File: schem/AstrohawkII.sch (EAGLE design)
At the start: 4 parts, among them J1 RASPBERRYPI-40-PIN-GPIO_PTH_N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

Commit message: updates eagle schematic and board
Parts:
- removed J3: (no value), SparkFun-Connectors:CONN_04PTH
- removed J4: (no value), SparkFun-Connectors:CONN_06SILK_FEMALE_PTH
- added U$1: BNO055, rocketry:BNO055
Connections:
- removed net 3VO: J2.3, J4.2
- removed net ADR: J3.4
- removed net PS0: J3.1
- removed net PS1: J3.2
- net GND: no longer J4.3
- net INT: now also J1.GP5; no longer J3.3
- net INT1: now also J1.GP12
- net INT2: now also J1.GP13
- net RST: now also J1.GP6; no longer J4.6
- net SCL: no longer J4.5
- net SDA: no longer J4.4
- net VIN: no longer J4.1
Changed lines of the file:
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@@
 <attribute name="MPL3115A2" value=""/>
 </part>
-<part name="J3" library="SparkFun-Connectors" deviceset="CONN_04" device="PTH">
-<attribute name="BNO055X04" value=""/>
-</part>
-<part name="J4" library="SparkFun-Connectors" deviceset="CONN_06" device="SILK_FEMALE_PTH">
-<attribute name="BNO055X06" value=""/>
-</part>
+<part name="U$1" library="rocketry" deviceset="BNO055" device=""/>
 </parts>
 <sheets>
@@
 <attribute name="MPL3115A2" x="73.66" y="78.74" size="1.778" layer="96" display="name"/>
 </instance>
-<instance part="J3" gate="J1" x="78.74" y="66.04" smashed="yes">
-<attribute name="VALUE" x="73.66" y="58.674" size="1.778" layer="96" font="vector"/>
-<attribute name="NAME" x="73.66" y="74.168" size="1.778" layer="95" font="vector"/>
-<attribute name="BNO055X04" x="73.66" y="58.42" size="1.778" layer="96" display="name"/>
-</instance>
-<instance part="J4" gate="G$1" x="78.74" y="43.18" smashed="yes">
-<attribute name="VALUE" x="73.66" y="33.274" size="1.778" layer="96" font="vector"/>
-<attribute name="NAME" x="73.66" y="53.848" size="1.778" layer="95" font="vector"/>
-<attribute name="BNO055X06" x="73.66" y="33.02" size="1.778" layer="96" display="name"/>
+<instance part="U$1" gate="G$1" x="116.84" y="35.56" smashed="yes">
+<attribute name="NAME" x="114.3" y="58.42" size="1.778" layer="95"/>
+<attribute name="VALUE" x="114.3" y="17.78" size="1.778" layer="96"/>
 </instance>
 </instances>
@@
 <net name="PS0" class="0">
 <segment>
-<pinref part="J3" gate="J1" pin="1"/>
-<wire x1="83.82" y1="63.5" x2="91.44" y2="63.5" width="0.1524" layer="91"/>
-<label x="88.9" y="63.5" size="1.778" layer="95" align="bottom-right"/>
+<wire x1="137.16" y1="48.26" x2="144.78" y2="48.26" width="0.1524" layer="91"/>
+<label x="149.86" y="48.26" size="1.778" layer="95" align="bottom-right"/>
 </segment>
 </net>
 <net name="PS1" class="0">
 <segment>
-<pinref part="J3" gate="J1" pin="2"/>
-<wire x1="83.82" y1="66.04" x2="91.44" y2="66.04" width="0.1524" layer="91"/>
-<label x="88.9" y="66.04" size="1.778" layer="95" align="bottom-right"/>
+<wire x1="137.16" y1="43.18" x2="144.78" y2="43.18" width="0.1524" layer="91"/>
+<label x="149.86" y="43.18" size="1.778" layer="95" align="bottom-right"/>
 </segment>
 </net>
 <net name="INT" class="0">
 <segment>
-<pinref part="J3" gate="J1" pin="3"/>
-<wire x1="83.82" y1="68.58" x2="91.44" y2="68.58" width="0.1524" layer="91"/>
-<label x="88.9" y="68.58" size="1.778" layer="95" align="bottom-right"/>
+<wire x1="137.16" y1="38.1" x2="144.78" y2="38.1" width="0.1524" layer="91"/>
+<label x="149.86" y="38.1" size="1.778" layer="95" align="bottom-right"/>
+</segment>
+<segment>
+<pinref part="J1" gate="G$1" pin="GP5"/>
+<wire x1="10.16" y1="86.36" x2="2.54" y2="86.36" width="0.1524" layer="91"/>
+<label x="0" y="86.36" size="1.778" layer="95"/>
 </segment>
 </net>
 <net name="ADR" class="0">
 <segment>
-<pinref part="J3" gate="J1" pin="4"/>
-<wire x1="83.82" y1="71.12" x2="91.44" y2="71.12" width="0.1524" layer="91"/>
-<label x="88.9" y="71.12" size="1.778" layer="95" align="bottom-right"/>
+<wire x1="137.16" y1="33.02" x2="144.78" y2="33.02" width="0.1524" layer="91"/>
+<label x="144.78" y="33.02" size="1.778" layer="95" rot="MR0" align="bottom-right"/>
 </segment>
 </net>
@@
 </segment>
 <segment>
-<pinref part="J4" gate="G$1" pin="1"/>
-<wire x1="83.82" y1="38.1" x2="91.44" y2="38.1" width="0.1524" layer="91"/>
-<label x="88.9" y="38.1" size="1.778" layer="95" align="bottom-right"/>
+<wire x1="93.98" y1="50.8" x2="101.6" y2="50.8" width="0.1524" layer="91"/>
+<label x="93.98" y="50.8" size="1.778" layer="95" align="bottom-right"/>
 </segment>
 <segment>
@@
 </segment>
 <segment>
-<pinref part="J4" gate="G$1" pin="3"/>
-<wire x1="83.82" y1="43.18" x2="91.44" y2="43.18" width="0.1524" layer="91"/>
-<label x="88.9" y="43.18" size="1.778" layer="95" align="bottom-right"/>
+<wire x1="93.98" y1="40.64" x2="101.6" y2="40.64" width="0.1524" layer="91"/>
+<label x="93.98" y="40.64" size="1.778" layer="95" align="bottom-right"/>
 </segment>
 <segment>
@@
 <wire x1="10.16" y1="43.18" x2="-5.08" y2="43.18" width="0.1524" layer="91"/>
 <label x="-2.54" y="43.18" size="1.778" layer="95"/>
-</segment>
-</net>
-<net name="3VO" class="0">
-<segment>
-<pinref part="J2" gate="J1" pin="3"/>
-<wire x1="83.82" y1="88.9" x2="91.44" y2="88.9" width="0.1524" layer="91"/>
-<label x="88.9" y="88.9" size="1.778" layer="95" align="bottom-right"/>
-</segment>
-<segment>
-<pinref part="J4" gate="G$1" pin="2"/>
-<wire x1="83.82" y1="40.64" x2="91.44" y2="40.64" width="0.1524" layer="91"/>
-<label x="88.9" y="40.64" size="1.778" layer="95" align="bottom-right"/>
 </segment>
 </net>
@@
 <label x="88.9" y="91.44" size="1.778" layer="95" align="bottom-right"/>
 </segment>
+<segment>
+<pinref part="J1" gate="G$1" pin="GP13"/>
+<wire x1="10.16" y1="78.74" x2="2.54" y2="78.74" width="0.1524" layer="91"/>
+<label x="0" y="78.74" size="1.778" layer="95"/>
+</segment>
 </net>
 <net name="INT1" class="0">
@@
 <wire x1="83.82" y1="93.98" x2="91.44" y2="93.98" width="0.1524" layer="91"/>
 <label x="88.9" y="93.98" size="1.778" layer="95" align="bottom-right"/>
+</segment>
+<segment>
+<pinref part="J1" gate="G$1" pin="GP12"/>
+<wire x1="10.16" y1="81.28" x2="2.54" y2="81.28" width="0.1524" layer="91"/>
+<label x="0" y="81.28" size="1.778" layer="95"/>
 </segment>
 </net>
@@
 </segment>
 <segment>
-<pinref part="J4" gate="G$1" pin="5"/>
-<wire x1="83.82" y1="48.26" x2="91.44" y2="48.26" width="0.1524" layer="91"/>
-<label x="88.9" y="48.26" size="1.778" layer="95" align="bottom-right"/>
+<wire x1="93.98" y1="30.48" x2="101.6" y2="30.48" width="0.1524" layer="91"/>
+<label x="93.98" y="30.48" size="1.778" layer="95" align="bottom-right"/>
 </segment>
 <segment>
@@
 </segment>
 <segment>
-<pinref part="J4" gate="G$1" pin="4"/>
-<wire x1="83.82" y1="45.72" x2="91.44" y2="45.72" width="0.1524" layer="91"/>
-<label x="88.9" y="45.72" size="1.778" layer="95" align="bottom-right"/>
+<wire x1="93.98" y1="35.56" x2="101.6" y2="35.56" width="0.1524" layer="91"/>
+<label x="93.98" y="35.56" size="1.778" layer="95" align="bottom-right"/>
 </segment>
 <segment>
@@
 <net name="RST" class="0">
 <segment>
-<pinref part="J4" gate="G$1" pin="6"/>
-<wire x1="83.82" y1="50.8" x2="91.44" y2="50.8" width="0.1524" layer="91"/>
-<label x="88.9" y="50.8" size="1.778" layer="95" align="bottom-right"/>
+<wire x1="93.98" y1="25.4" x2="101.6" y2="25.4" width="0.1524" layer="91"/>
+<label x="93.98" y="25.4" size="1.778" layer="95" align="bottom-right"/>
+</segment>
+<segment>
+<pinref part="J1" gate="G$1" pin="GP6"/>
+<wire x1="10.16" y1="83.82" x2="2.54" y2="83.82" width="0.1524" layer="91"/>
+<label x="0" y="83.82" size="1.778" layer="95"/>
 </segment>
 </net>

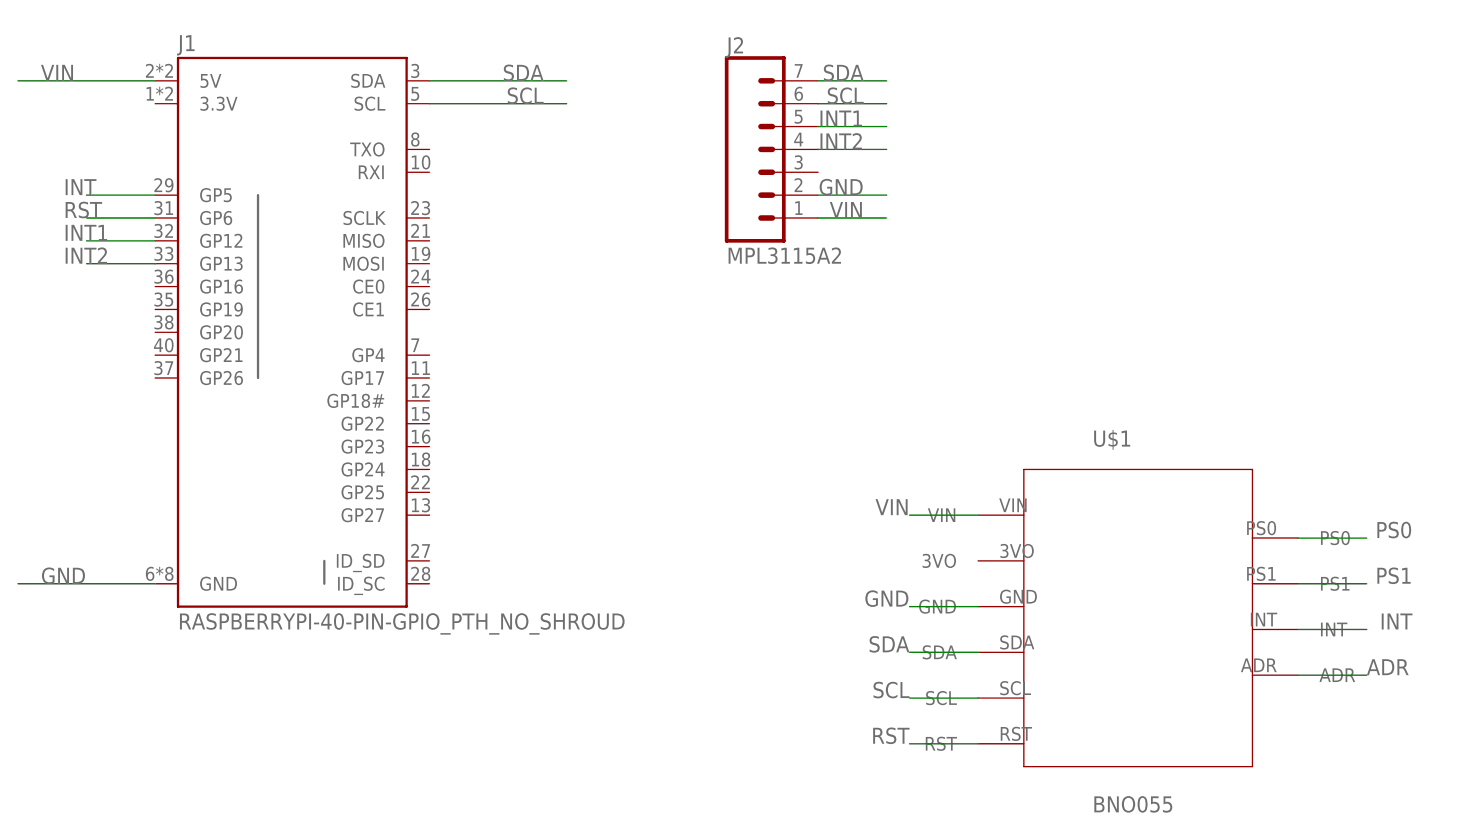
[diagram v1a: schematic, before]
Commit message: fixes holes for raspberry pi
This change fixes the holes for the raspberry pi, adds
measurement lines showing the correct dimensions, and
updates the IMU part because the pins were backwards on
the symbol.
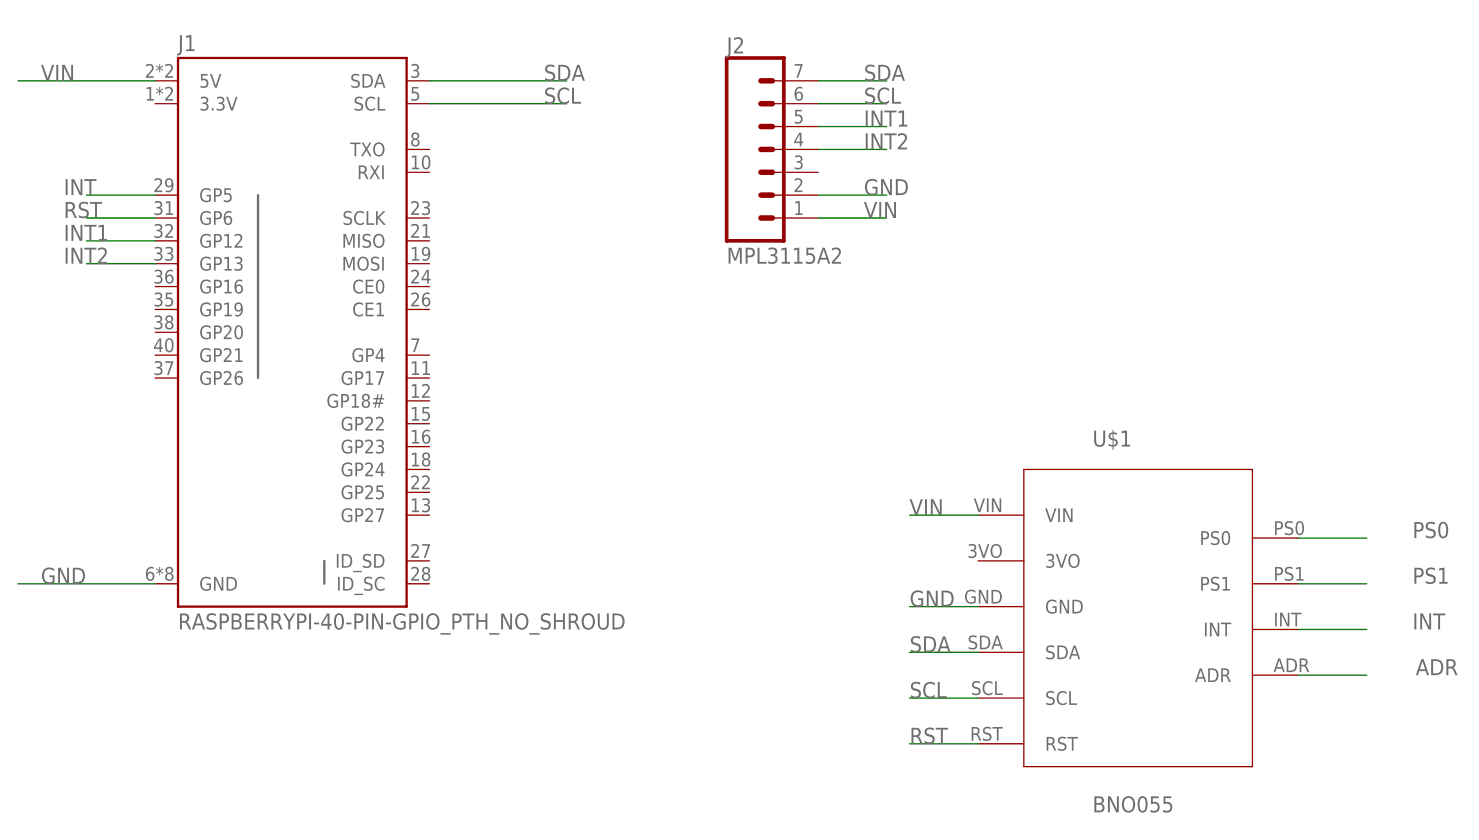
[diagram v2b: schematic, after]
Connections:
- new net ADR: U$1.ADR
- new net PS0: U$1.PS0
- new net PS1: U$1.PS1
- net GND: now also U$1.GND
- net INT: now also U$1.INT
- net RST: now also U$1.RST
- net SCL: now also U$1.SCL
- net SDA: now also U$1.SDA
- net VIN: now also U$1.VIN
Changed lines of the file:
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@@
 <?xml version="1.0" encoding="utf-8"?>
 <!DOCTYPE eagle SYSTEM "eagle.dtd">
-<eagle version="9.5.2">
+<eagle version="8.2.2">
 <drawing>
 <settings>
@@
 <attribute name="MPL3115A2" x="73.66" y="78.74" size="1.778" layer="96" display="name"/>
 </instance>
-<instance part="U$1" gate="G$1" x="116.84" y="35.56" smashed="yes">
-<attribute name="NAME" x="114.3" y="58.42" size="1.778" layer="95"/>
-<attribute name="VALUE" x="114.3" y="17.78" size="1.778" layer="96"/>
-</instance>
+<instance part="U$1" gate="G$1" x="116.84" y="35.56"/>
 </instances>
 <busses>
@@
 <segment>
 <wire x1="137.16" y1="48.26" x2="144.78" y2="48.26" width="0.1524" layer="91"/>
-<label x="149.86" y="48.26" size="1.778" layer="95" align="bottom-right"/>
+<label x="149.86" y="48.26" size="1.778" layer="95"/>
+<pinref part="U$1" gate="G$1" pin="PS0"/>
 </segment>
 </net>
@@
 <segment>
 <wire x1="137.16" y1="43.18" x2="144.78" y2="43.18" width="0.1524" layer="91"/>
-<label x="149.86" y="43.18" size="1.778" layer="95" align="bottom-right"/>
+<label x="149.86" y="43.18" size="1.778" layer="95"/>
+<pinref part="U$1" gate="G$1" pin="PS1"/>
 </segment>
 </net>
@@
 <segment>
 <wire x1="137.16" y1="38.1" x2="144.78" y2="38.1" width="0.1524" layer="91"/>
-<label x="149.86" y="38.1" size="1.778" layer="95" align="bottom-right"/>
+<label x="149.86" y="38.1" size="1.778" layer="95"/>
+<pinref part="U$1" gate="G$1" pin="INT"/>
 </segment>
 <segment>
@@
 <segment>
 <wire x1="137.16" y1="33.02" x2="144.78" y2="33.02" width="0.1524" layer="91"/>
-<label x="144.78" y="33.02" size="1.778" layer="95" rot="MR0" align="bottom-right"/>
+<label x="154.94" y="33.02" size="1.778" layer="95" rot="MR0"/>
+<pinref part="U$1" gate="G$1" pin="ADR"/>
 </segment>
 </net>
@@
 <pinref part="J2" gate="J1" pin="1"/>
 <wire x1="83.82" y1="83.82" x2="91.44" y2="83.82" width="0.1524" layer="91"/>
-<label x="88.9" y="83.82" size="1.778" layer="95" align="bottom-right"/>
+<label x="88.9" y="83.82" size="1.778" layer="95"/>
 </segment>
 <segment>
 <wire x1="93.98" y1="50.8" x2="101.6" y2="50.8" width="0.1524" layer="91"/>
-<label x="93.98" y="50.8" size="1.778" layer="95" align="bottom-right"/>
+<label x="93.98" y="50.8" size="1.778" layer="95"/>
+<pinref part="U$1" gate="G$1" pin="VIN"/>
 </segment>
 <segment>
@@
 <pinref part="J2" gate="J1" pin="2"/>
 <wire x1="83.82" y1="86.36" x2="91.44" y2="86.36" width="0.1524" layer="91"/>
-<label x="88.9" y="86.36" size="1.778" layer="95" align="bottom-right"/>
+<label x="88.9" y="86.36" size="1.778" layer="95"/>
 </segment>
 <segment>
 <wire x1="93.98" y1="40.64" x2="101.6" y2="40.64" width="0.1524" layer="91"/>
-<label x="93.98" y="40.64" size="1.778" layer="95" align="bottom-right"/>
+<label x="93.98" y="40.64" size="1.778" layer="95"/>
+<pinref part="U$1" gate="G$1" pin="GND"/>
 </segment>
 <segment>
@@
 <pinref part="J2" gate="J1" pin="4"/>
 <wire x1="83.82" y1="91.44" x2="91.44" y2="91.44" width="0.1524" layer="91"/>
-<label x="88.9" y="91.44" size="1.778" layer="95" align="bottom-right"/>
+<label x="88.9" y="91.44" size="1.778" layer="95"/>
 </segment>
 <segment>
@@
 <pinref part="J2" gate="J1" pin="5"/>
 <wire x1="83.82" y1="93.98" x2="91.44" y2="93.98" width="0.1524" layer="91"/>
-<label x="88.9" y="93.98" size="1.778" layer="95" align="bottom-right"/>
+<label x="88.9" y="93.98" size="1.778" layer="95"/>
 </segment>
 <segment>
@@
 <pinref part="J2" gate="J1" pin="6"/>
 <wire x1="83.82" y1="96.52" x2="91.44" y2="96.52" width="0.1524" layer="91"/>
-<label x="88.9" y="96.52" size="1.778" layer="95" align="bottom-right"/>
+<label x="88.9" y="96.52" size="1.778" layer="95"/>
 </segment>
 <segment>
 <wire x1="93.98" y1="30.48" x2="101.6" y2="30.48" width="0.1524" layer="91"/>
-<label x="93.98" y="30.48" size="1.778" layer="95" align="bottom-right"/>
+<label x="93.98" y="30.48" size="1.778" layer="95"/>
+<pinref part="U$1" gate="G$1" pin="SCL"/>
 </segment>
 <segment>
 <pinref part="J1" gate="G$1" pin="SCL"/>
 <wire x1="40.64" y1="96.52" x2="55.88" y2="96.52" width="0.1524" layer="91"/>
-<label x="53.34" y="96.52" size="1.778" layer="95" align="bottom-right"/>
+<label x="53.34" y="96.52" size="1.778" layer="95"/>
 </segment>
 </net>
@@
 <pinref part="J2" gate="J1" pin="7"/>
 <wire x1="83.82" y1="99.06" x2="91.44" y2="99.06" width="0.1524" layer="91"/>
-<label x="88.9" y="99.06" size="1.778" layer="95" align="bottom-right"/>
+<label x="88.9" y="99.06" size="1.778" layer="95"/>
 </segment>
 <segment>
 <wire x1="93.98" y1="35.56" x2="101.6" y2="35.56" width="0.1524" layer="91"/>
-<label x="93.98" y="35.56" size="1.778" layer="95" align="bottom-right"/>
+<label x="93.98" y="35.56" size="1.778" layer="95"/>
+<pinref part="U$1" gate="G$1" pin="SDA"/>
 </segment>
 <segment>
 <pinref part="J1" gate="G$1" pin="SDA"/>
 <wire x1="40.64" y1="99.06" x2="55.88" y2="99.06" width="0.1524" layer="91"/>
-<label x="53.34" y="99.06" size="1.778" layer="95" align="bottom-right"/>
+<label x="53.34" y="99.06" size="1.778" layer="95"/>
 </segment>
 </net>
@@
 <segment>
 <wire x1="93.98" y1="25.4" x2="101.6" y2="25.4" width="0.1524" layer="91"/>
-<label x="93.98" y="25.4" size="1.778" layer="95" align="bottom-right"/>
+<label x="93.98" y="25.4" size="1.778" layer="95"/>
+<pinref part="U$1" gate="G$1" pin="RST"/>
 </segment>
 <segment>
@@
 </schematic>
 </drawing>
-<compatibility>
-<note version="9.0" severity="warning">
-Since Version 9.0, EAGLE supports the align property for labels.
-Labels in schematic will not be understood with this version. Update EAGLE to the latest version
-for full support of labels.
-</note>
-</compatibility>
 </eagle>

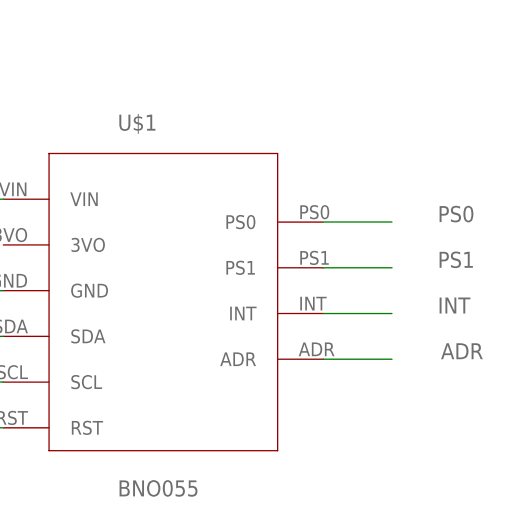
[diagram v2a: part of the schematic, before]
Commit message: finishes placement and routes wires
This change places the raspberry pi header in the
correct location. It also routes wires to all
relevant locations. For some reason the raspberry
pi header we're using wants to connect all of the
power and ground pins together, but that shouldn't
be necessary, so I've left them unconnected and
they show as air wires.
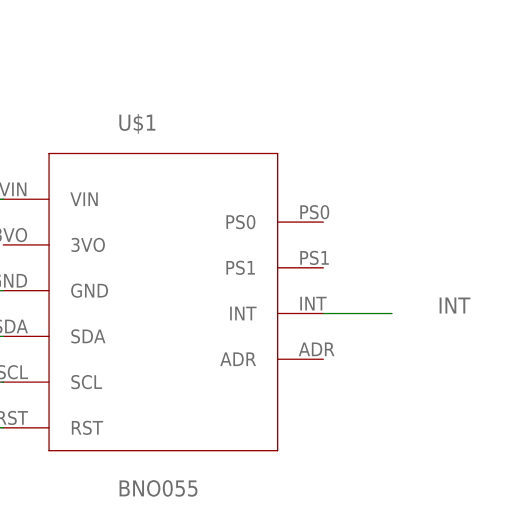
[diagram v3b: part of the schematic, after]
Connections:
- removed net ADR: U$1.ADR
- removed net PS0: U$1.PS0
- removed net PS1: U$1.PS1
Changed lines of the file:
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@@
 </busses>
 <nets>
-<net name="PS0" class="0">
-<segment>
-<wire x1="137.16" y1="48.26" x2="144.78" y2="48.26" width="0.1524" layer="91"/>
-<label x="149.86" y="48.26" size="1.778" layer="95"/>
-<pinref part="U$1" gate="G$1" pin="PS0"/>
-</segment>
-</net>
-<net name="PS1" class="0">
-<segment>
-<wire x1="137.16" y1="43.18" x2="144.78" y2="43.18" width="0.1524" layer="91"/>
-<label x="149.86" y="43.18" size="1.778" layer="95"/>
-<pinref part="U$1" gate="G$1" pin="PS1"/>
-</segment>
-</net>
 <net name="INT" class="0">
 <segment>
@@
 <wire x1="10.16" y1="86.36" x2="2.54" y2="86.36" width="0.1524" layer="91"/>
 <label x="0" y="86.36" size="1.778" layer="95"/>
-</segment>
-</net>
-<net name="ADR" class="0">
-<segment>
-<wire x1="137.16" y1="33.02" x2="144.78" y2="33.02" width="0.1524" layer="91"/>
-<label x="154.94" y="33.02" size="1.778" layer="95" rot="MR0"/>
-<pinref part="U$1" gate="G$1" pin="ADR"/>
 </segment>
 </net>
@@
 </sheet>
 </sheets>
+<errors>
+</errors>
 </schematic>
 </drawing>
